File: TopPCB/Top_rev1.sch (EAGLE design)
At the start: 5 parts, among them IC1 74HC595D

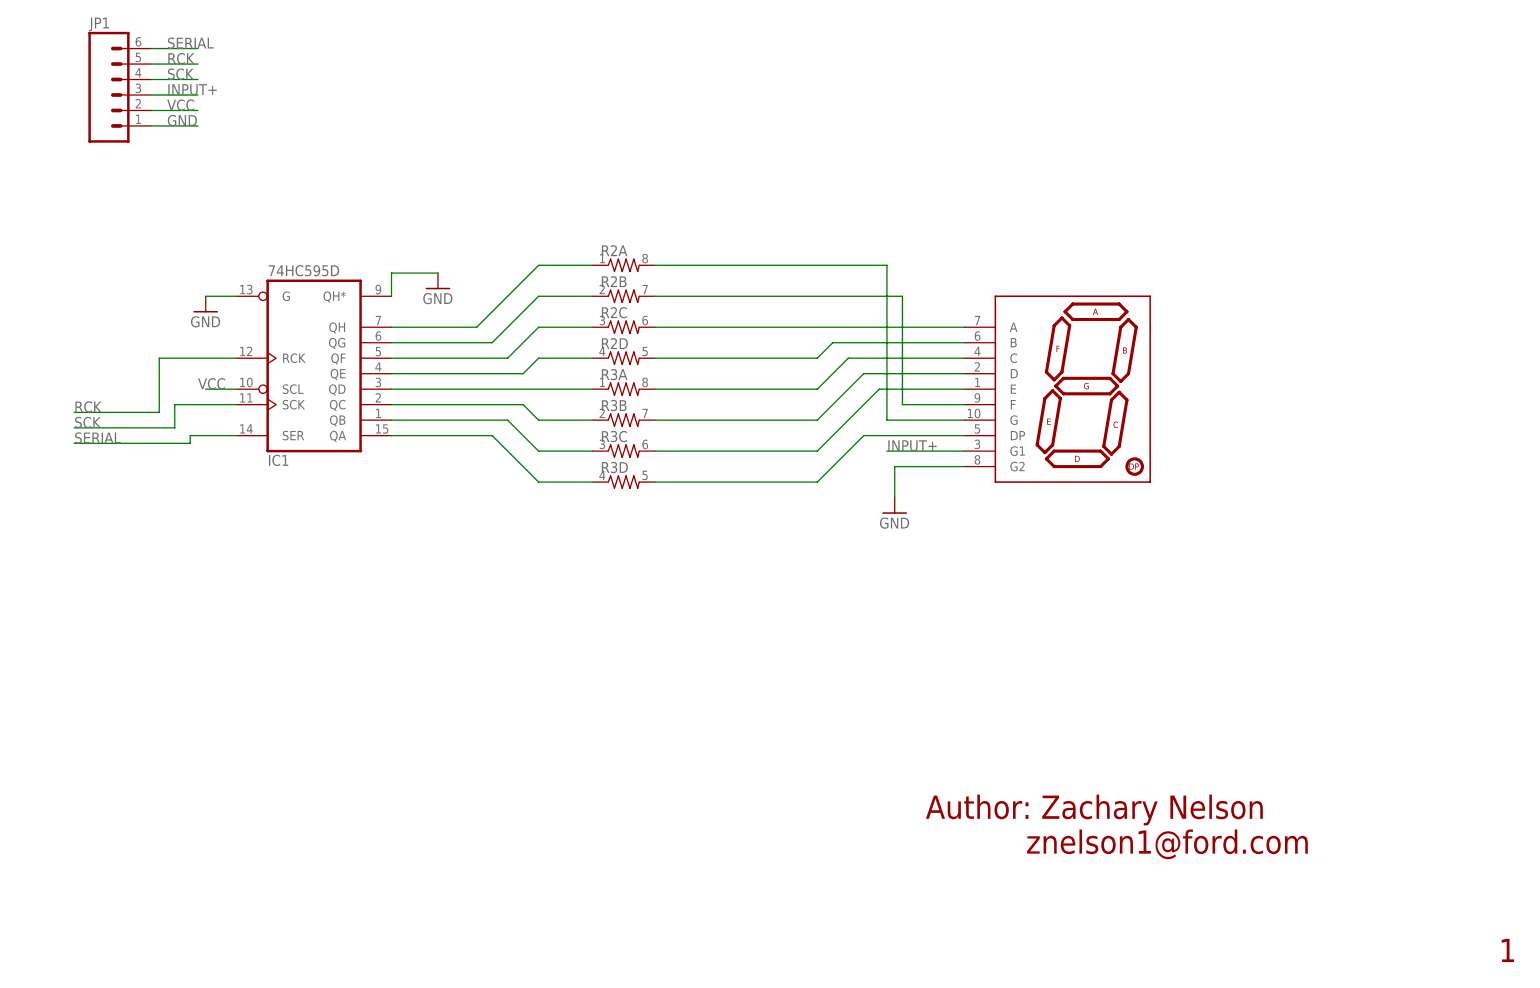
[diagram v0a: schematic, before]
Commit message: layout board and route traces. changed a few signals between shift register and 7 segment
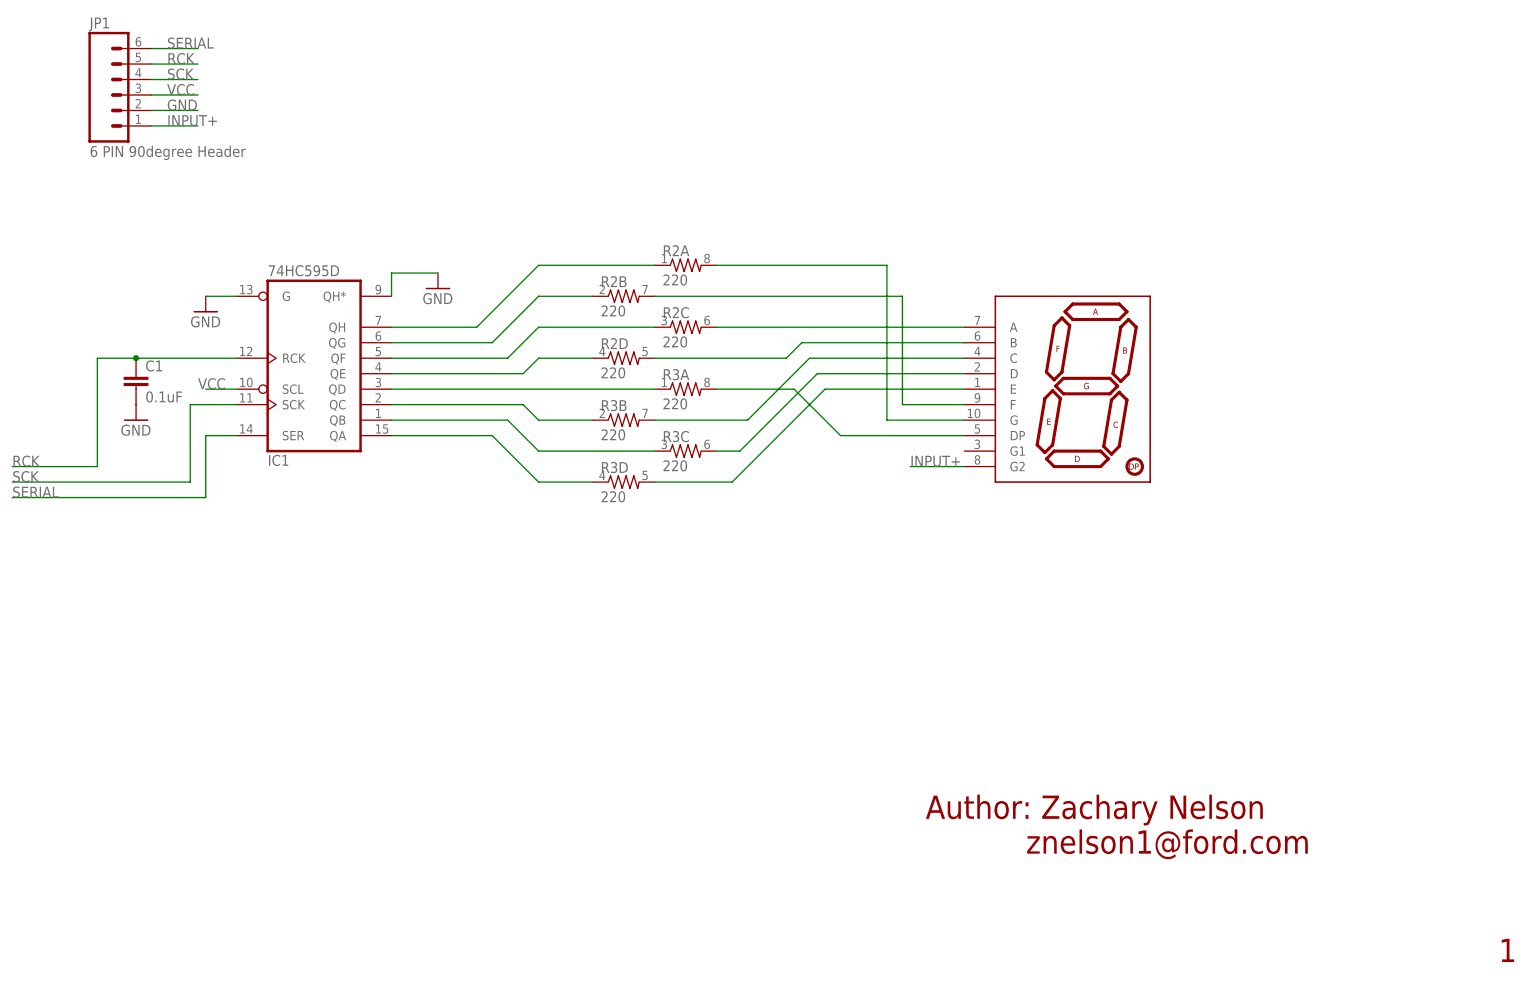
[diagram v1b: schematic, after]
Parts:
- added C1: 0.1uF, SparkFun-Capacitors:CAP0402-CAP
- JP1: value (none) -> 6 PIN 90degree Header
- R2, R3: value (none) -> 220
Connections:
- removed net N$6: R3B.2, U$1.D
- new net N$19: R3C.2, U$1.D
- net GND: now also C1.2, JP1.2; no longer JP1.1, U$1.G2
- net INPUT+: now also JP1.1, U$1.G2; no longer JP1.3, U$1.G1
- net N$1: now also R3A.2; no longer R3D.2
- net N$3: now also R3D.2; no longer R3C.2
- net N$7: now also R3B.2; no longer R3A.2
- net RCK: now also C1.1
- net VCC: now also JP1.3; no longer JP1.2
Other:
- moved on the sheet: R2A, R2C, R3A, R3C

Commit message: remove ground connection on pin 9 of shift register
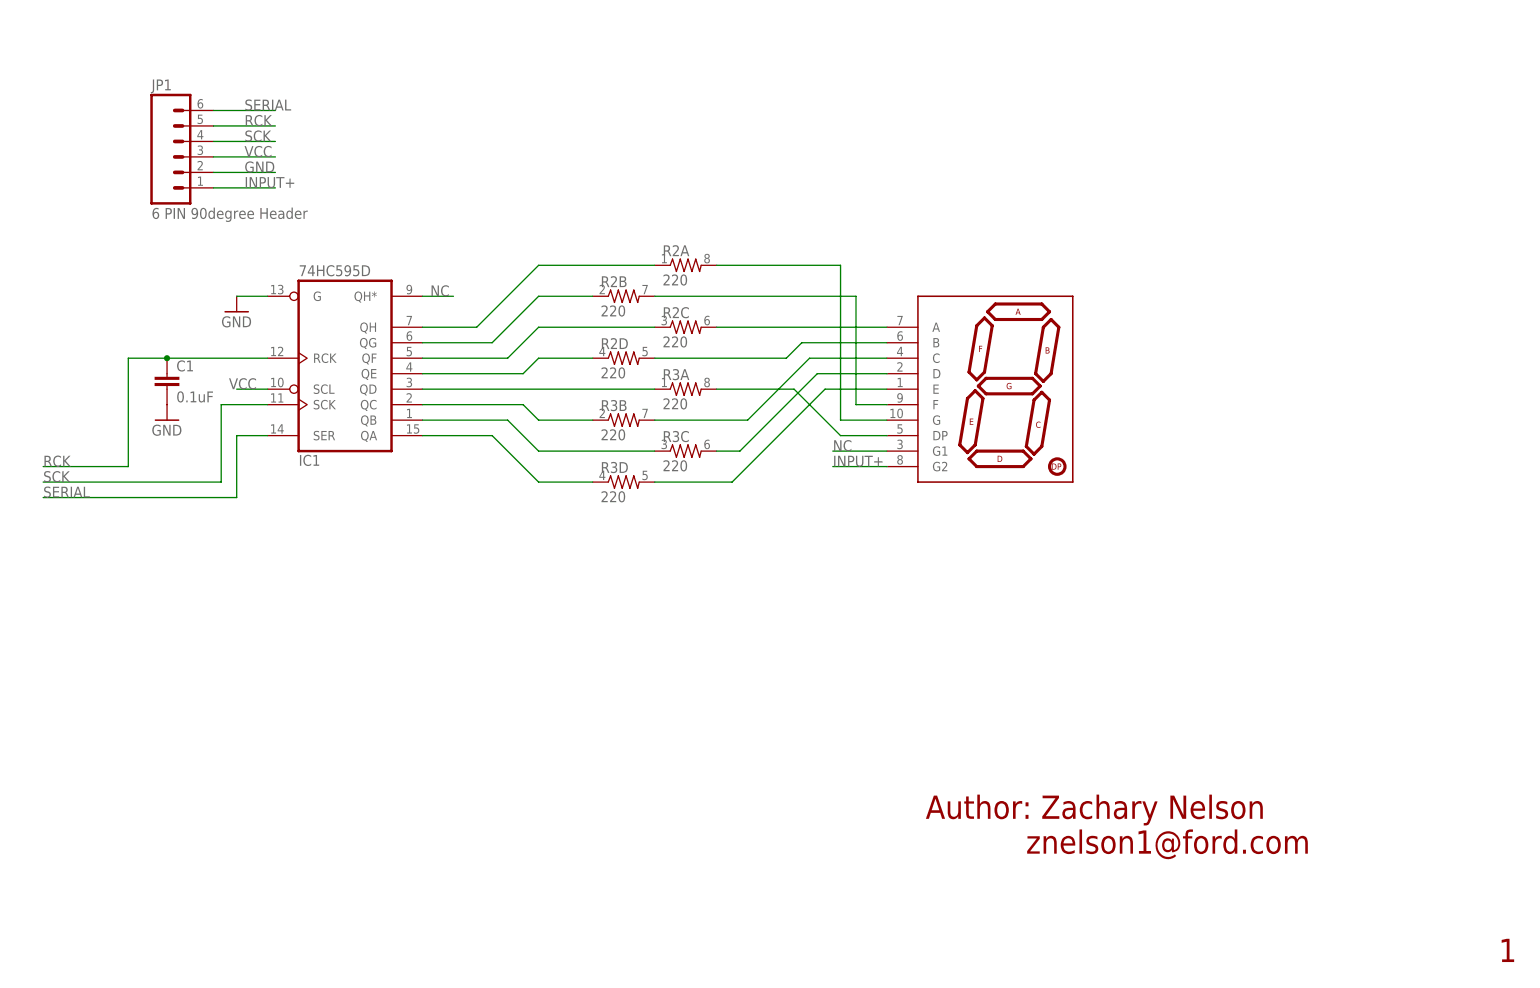
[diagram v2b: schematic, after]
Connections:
- new net NC: IC1A.QH*, U$1.G1
- net GND: no longer IC1A.QH*
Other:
- moved on the sheet: C1, IC1, JP1

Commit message: remove BottomPCB folder, finished version 1 of TopPCB, moved Bottom_rev1 to TopPCB folder, first commit of Bottom pcb work.
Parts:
- removed R2, R3: 220, SparkFun-Resistors:RESISTOR-ARRAY0603-ARV
- added RN1, RN2: 220, resistor-array:744-8
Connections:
- removed net NC: IC1A.QH*, U$1.G1
- new net NC1: U$1.G1
- new net NC2: IC1A.QH*
- net N$1: now also RN2.8; no longer R3A.2
- net N$10: now also RN1.4; no longer R2D.1
- net N$11: now also RN1.3; no longer R2C.1
- net N$12: now also RN1.2; no longer R2B.1
- net N$13: now also RN1.1; no longer R2A.1
- net N$14: now also RN1.6; no longer R2C.2
- net N$15: now also RN1.7; no longer R2B.2
- net N$16: now also RN1.8; no longer R2A.2
- net N$19: now also RN2.6; no longer R3C.2
- net N$2: now also RN2.3; no longer R3C.1
- net N$3: now also RN2.5; no longer R3D.2
- net N$4: now also RN2.2; no longer R3B.1
- net N$5: now also RN2.1; no longer R3A.1
- net N$7: now also RN2.7; no longer R3B.2
- net N$8: now also RN1.5; no longer R2D.2
- net N$9: now also RN2.4; no longer R3D.1
